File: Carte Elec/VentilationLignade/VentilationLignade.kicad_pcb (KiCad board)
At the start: 2 copper layers, 28 parts, among them P1 RelaisBoard1, P10 SDCard, P11 Codeur Rotatif, P12 Teensy dessous, P13 EndStops1, P14 Teensy_Haut, P15 EndStops2, P16 Teensy_cote, P17 Retour 12V, P18 Masse_12V, P19 12V1, P2 Temp_Ext, P20 12V2, P21 12V_1et2, P22 Teensy_Bas, P3 RelaisBoard2, P4 Temp_Int, P5 RelaisBoard3, P6 Temp_Chem, P7 RelaisBoard4, P8 RelaisBoard5, P9 TFT, SW1 Reset_Push, SW2 BackLight_On/ff

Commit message: Dessin de carte. Changement des pins pour avoir un truc cohérent au niveau de la carte.
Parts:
- C1, C2, C3: moved to B.Cu
- moved P12 216.8 mm to (0.00, 0.00)
- moved P18 114.1 mm to (262.9, 200.7)
- moved P19 102.6 mm to (269.2, 157.5), turned to 90 degrees
- moved P20 101.3 mm to (269.2, 149.9), turned to 90 degrees
- moved P21 97.1 mm to (241.3, 200.7), turned to 180 degrees
- moved P17 88.0 mm to (256.5, 143.5)
- moved P15 81.6 mm to (250.2, 143.5)
- moved P13 75.3 mm to (243.8, 143.5)
- moved P8 73.3 mm to (203.2, 200.7), turned to 180 degrees
- moved SW2 70.4 mm to (231.1, 168.9), turned to 90 degrees
- moved P7 68.3 mm to (190.5, 200.7), turned to 180 degrees
- moved P1 66.8 mm to (152.4, 200.7), turned to 180 degrees
- moved P5 65.4 mm to (177.8, 200.7), turned to 180 degrees
- moved P3 64.9 mm to (165.1, 200.7), turned to 180 degrees
- moved R1 60.2 mm to (222.2, 163.8), turned to 270 degrees
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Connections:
- P12 pad 1: 12V2_ON -> SELECT_12V
- P12 pad 10: ENCODEUR_B -> (no net)
- P12 pad 2: SELECT_12V -> (no net)
- P12 pad 3: 12V1_ON -> ENCODEUR_SW
- P12 pad 4: 12V_CHECK -> ENCODEUR_A
- P12 pad 5: SELECT_VMC -> ENCODEUR_B
- P12 pad 6: ENCODEUR_SW -> (no net)
- P12 pad 7: VENT_CAVE -> (no net)
- P12 pad 8: ENCODEUR_A -> (no net)
- P12 pad 9: VENT_CHEMINEE -> (no net)
- P14 pad 1: (no net) -> 12V_CHECK
- P22 pad 10: (no net) -> 12V2_ON
- P22 pad 2: (no net) -> BYPASS_1_F
- P22 pad 3: (no net) -> BYPASS_1_O
- P22 pad 4: (no net) -> BYPASS_2_F
- P22 pad 5: BYPASS_1_F -> BYPASS_2_O
- P22 pad 6: BYPASS_1_O -> VENT_CAVE
- P22 pad 7: BYPASS_2_F -> VENT_CHEMINEE
- P22 pad 8: BYPASS_2_O -> 12V1_ON
- P22 pad 9: (no net) -> SELECT_VMC
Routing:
- net GND: track 0.00 -> 230.6 mm, vias 0 -> 1
- net +5V: track 0.00 -> 165.6 mm
- net +3.3V: track 0.00 -> 129.4 mm
- net SPI_MISO: track 0.00 -> 116.7 mm
- net SPI_SCK: track 0.00 -> 83.7 mm
- net GNDPWR: track 0.00 -> 79.3 mm
- net 12V2: track 0.00 -> 69.4 mm
- net 12V1: track 0.00 -> 60.4 mm
- net TFT_DC: track 0.00 -> 47.4 mm
- net SPI_MOSI: track 0.00 -> 43.0 mm
- net TFT_CS: track 0.00 -> 36.2 mm
- net TEXT_CS: track 0.00 -> 30.4 mm
- net SELECT_VMC: track 0.00 -> 30.1 mm
- net BYPASS_1_O: track 0.00 -> 30.1 mm
- net BYPASS_1_F: track 0.00 -> 30.1 mm
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- added copper zone on F.Cu, net GND
- added copper zone on F.Cu, net GNDPWR
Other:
- net class 12V added: clearance 0.3, trace_width 1, via_dia 0.889, via_drill 0.635

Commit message: Ajout d'un RS232 MAX au cas ou.
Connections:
- P12 pad 2: (no net) -> ENCODEUR_SW
- P12 pad 3: ENCODEUR_SW -> (no net)
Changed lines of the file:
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@@
     (links 76)
     (no_connects 11)
-    (area 0 0 0 0)
+    (area -10.650501 -4.8085 271.830001 204.520001)
     (thickness 1.6)
     (drawings 4)
@@
     (pad 2 thru_hole circle (at -5.08 3.81) (size 1.397 1.397) (drill 0.8128)
       (layers *.Cu *.Mask Dessus.SilkS)
+      (net 14 ENCODEUR_SW)
     )
     (pad 3 thru_hole circle (at -2.54 3.81) (size 1.397 1.397) (drill 0.8128)
       (layers *.Cu *.Mask Dessus.SilkS)
-      (net 14 ENCODEUR_SW)
     )
     (pad 4 thru_hole circle (at 0 3.81) (size 1.397 1.397) (drill 0.8128)
@@
   (segment (start 157.48 203.2) (end 166.37 203.2) (width 0.254) (layer Dessus.Cu) (net 19))
   (segment (start 156.21 201.93) (end 157.48 203.2) (width 0.254) (layer Dessus.Cu) (net 19))
-  (segment (start 266.7 200.66) (end 268.605 198.755) (width 1) (layer Dessus.Cu) (net 20) (status 400000))
+  (segment (start 266.7 200.66) (end 268.605 198.755) (width 1) (layer Dessus.Cu) (net 20))
   (segment (start 271.145 161.29) (end 271.145 154.305) (width 1) (layer Dessus.Cu) (net 20))
   (segment (start 268.605 163.83) (end 271.145 161.29) (width 1) (layer Dessus.Cu) (net 20))
   (segment (start 268.605 198.755) (end 268.605 163.83) (width 1) (layer Dessus.Cu) (net 20))
-  (segment (start 264.16 200.66) (end 266.7 200.66) (width 1) (layer Dessus.Cu) (net 20) (status C00000))
-  (segment (start 261.62 200.66) (end 264.16 200.66) (width 1) (layer Dessus.Cu) (net 20) (status C00000))
-  (segment (start 259.08 200.66) (end 261.62 200.66) (width 1) (layer Dessus.Cu) (net 20) (status C00000))
+  (segment (start 264.16 200.66) (end 266.7 200.66) (width 1) (layer Dessus.Cu) (net 20))
+  (segment (start 261.62 200.66) (end 264.16 200.66) (width 1) (layer Dessus.Cu) (net 20))
+  (segment (start 259.08 200.66) (end 261.62 200.66) (width 1) (layer Dessus.Cu) (net 20))
   (segment (start 269.24 148.59) (end 270.51 148.59) (width 1) (layer Dessus.Cu) (net 20))
   (segment (start 270.51 148.59) (end 271.145 149.225) (width 1) (layer Dessus.Cu) (net 20))

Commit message: Reprise de la carte => Dimensions réduites 50x100mm
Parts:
- added C4: C, C2, F.Cu at (195.6, 248.9)
- added C5: C, C2, F.Cu at (227.1, 251.0)
- added C7: C, C2, F.Cu at (213.6, 264.2)
- added C8: C, C2, F.Cu at (221.0, 264.2)
- added P23: Serial, SIL-4, F.Cu at (223.5, 254.0)
- added P24: Temp_PuitC, SIL-5, F.Cu at (198.1, 219.7)
- added R2: R, R4, F.Cu at (232.7, 253.5)
- added R3: R, R4, F.Cu at (229.9, 253.5)
- added U1: MAX232, SO16W, F.Cu at (216.4, 256.5)
- C1, C2, C3: moved to F.Cu
- P12: value Teensy dessous -> Teensy Bottom; footprint DIP-14__300 -> SIL-10
- moved P12 316.0 mm to (188.0, 254.0)
- moved P20 81.1 mm to (243.2, 226.7)
- moved P19 79.9 mm to (243.2, 233.0)
- moved P13 78.1 mm to (226.7, 219.7)
- moved P15 78.1 mm to (233.0, 219.7)
- moved P17 78.1 mm to (239.4, 219.7)
- moved P10 77.7 mm to (195.6, 233.7)
- moved P2 76.9 mm to (184.2, 219.7)
- moved P4 76.9 mm to (170.2, 219.7)
- moved P6 76.9 mm to (156.2, 219.7)
- moved P9 76.2 mm to (203.2, 238.8)
- moved SW2 74.5 mm to (213.4, 241.3)
- moved C1 74.4 mm to (208.0, 258.3), turned to 0 degrees
- moved R1 73.7 mm to (208.3, 236.2)
- moved C2 70.7 mm to (208.0, 255.5), turned to 0 degrees
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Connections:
- P12 pad 2: ENCODEUR_SW -> ENCODEUR_A
- P12 pad 3: (no net) -> ENCODEUR_B
- P12 pad 4: ENCODEUR_A -> ENCODEUR_SW
- P12 pad 5: ENCODEUR_B -> RX
- P12 pad 6: (no net) -> TX
- P14 pad 7: (no net) -> TPUIT_CS
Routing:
- net ENDSTOP_2_2: track 0.00 -> 68.2 mm
- net ENDSTOP_2_1: track 0.00 -> 68.0 mm
- net 12V_CHECK: track 0.00 -> 66.8 mm
- net ENDSTOP_1_1: track 0.00 -> 66.3 mm
- net ENDSTOP_1_2: track 0.00 -> 66.2 mm
- net GND: track 230.6 -> 279.9 mm, vias 1 -> 0
- net 12V2_ON: track 0.00 -> 43.9 mm
- net TPUIT_CS: track 0.00 -> 42.7 mm
- net RX: track 0.00 -> 34.0 mm, vias 0 -> 1
- net TX: track 0.00 -> 33.0 mm, vias 0 -> 1
- net ENCODEUR_A: track 4.48 -> 35.5 mm
- net SELECT_12V: track 0.00 -> 30.8 mm
- net ENCODEUR_B: track 3.96 -> 31.2 mm
- net N-0000023: track 0.00 -> 25.5 mm
- net ENCODEUR_SW: track 3.43 -> 28.4 mm
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- added copper zone on B.Cu, net +3.3V
- added copper zone on B.Cu, net +5V
- removed copper zone on F.Cu, net GNDPWR
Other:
- net class 12V: clearance 0.3 -> 0.5; via_dia 0.889 -> 1.2
- net class Default: clearance 0.254 -> 0.35; trace_width 0.254 -> 0.35; via_dia 0.889 -> 1.2; via_drill 0.635 -> 0.8
- rule trace_clearance: 0.254 -> 0.35

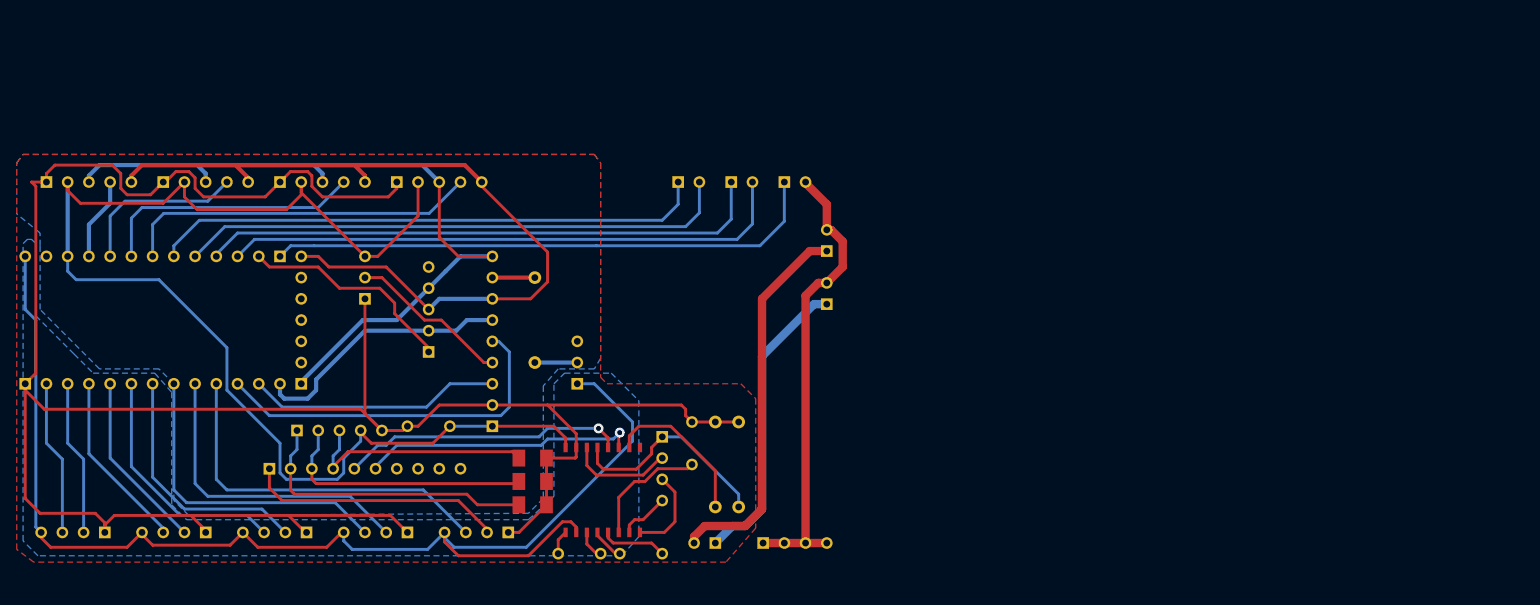
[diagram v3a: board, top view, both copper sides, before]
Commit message: Reprise de carte  : Suppression MAX232, pour avoir la place de mettre les MOC207
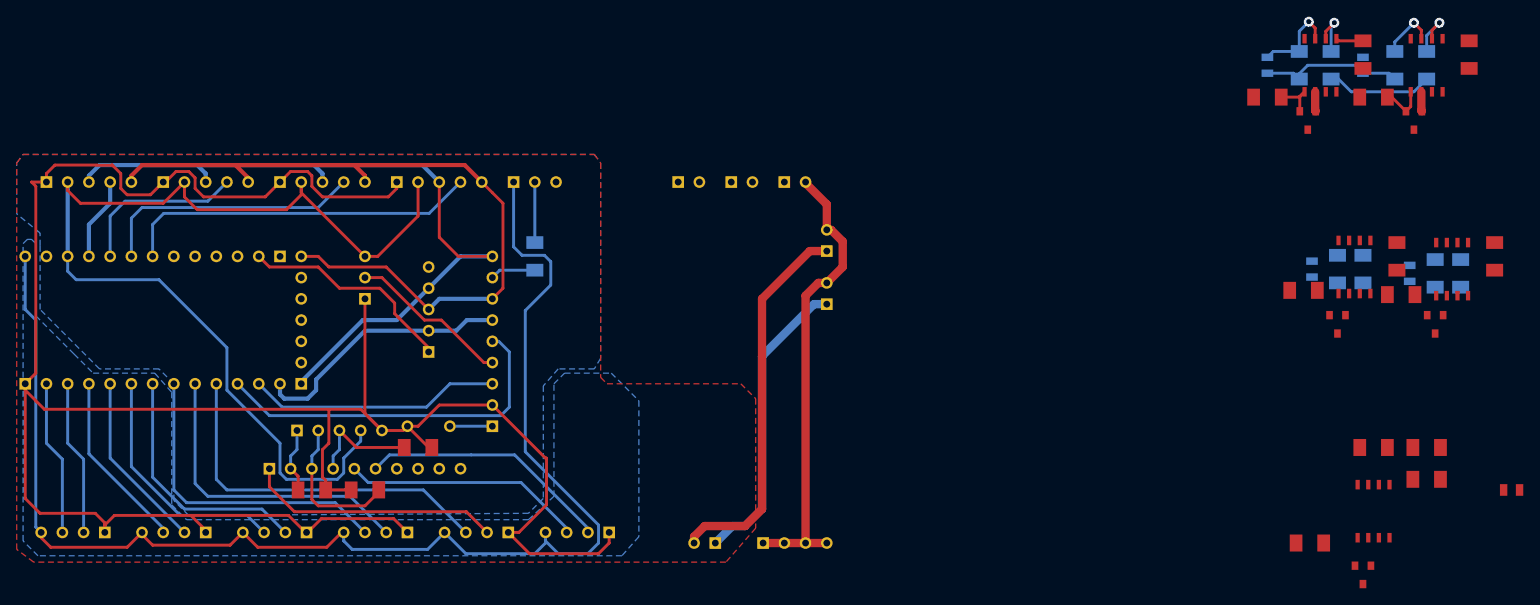
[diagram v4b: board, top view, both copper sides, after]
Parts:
- removed C5, C7, C8: C, C2
- removed R2, R3: R, R4
- removed U1: MAX232, SO16W
- added C10: C, SM0805, B.Cu at (312.9, 230.6)
- added C11: C, SM0805, F.Cu at (325.1, 256.5)
- added C12: C, SM0805, B.Cu at (295.9, 205.7)
- added C13: C, SM0805, B.Cu at (307.3, 205.7)
- added C9: C, SM0805, B.Cu at (301.2, 230.1)
- added D1: DIODE, SOT23, F.Cu at (304.3, 236.7)
- added D2: DIODE, SOT23, F.Cu at (316.0, 236.7)
- added D3: DIODE, SOT23, F.Cu at (307.3, 266.7)
- added D4: DIODE, SOT23, F.Cu at (300.7, 212.3)
- added D5: DIODE, SOT23, F.Cu at (313.4, 212.3)
- added R10: R, SM1206, B.Cu at (316.0, 230.6)
- added R11: R, SM1206, F.Cu at (315.0, 251.5)
- added R12: R, SM1206, B.Cu at (299.7, 205.7)
- added R13: R, SM1206, B.Cu at (311.1, 205.7)
- added R14: R, SM1206, B.Cu at (307.3, 230.1)
- added R15: R, SM1206, B.Cu at (319.0, 230.6)
- added R16: R, SM1206, F.Cu at (308.6, 251.5)
- added R17: R, SM1206, B.Cu at (303.5, 205.7)
- added R18: R, SM1206, B.Cu at (315.0, 205.7)
- added R19: R, SM1206, F.Cu at (311.4, 228.6)
- added R20: R, SM1206, F.Cu at (323.1, 228.6)
- added R21: R, SM1206, F.Cu at (315.0, 255.3)
- added R22: R, SM1206, F.Cu at (307.3, 204.5)
- added R23: R, SM1206, F.Cu at (320.0, 204.5)
- added R4: R, SM1206, F.Cu at (300.2, 232.7)
- added R5: R, SM1206, F.Cu at (311.9, 233.2)
- added R6: R, SM1206, F.Cu at (301.0, 262.9)
- added R7: R, SM1206, F.Cu at (295.9, 209.6)
- added R8: R, SM1206, F.Cu at (308.6, 209.6)
- added R9: R, SM1206, B.Cu at (304.3, 230.1)
- added U2: OPTO-TRANSISTOR, SO8N, F.Cu at (306.3, 229.9)
- added U3: OPTO-TRANSISTOR, SO8N, F.Cu at (318.0, 230.1)
- added U4: OPTO-TRANSISTOR, SO8N, F.Cu at (308.6, 259.1)
- added U5: OPTO-TRANSISTOR, SO8N, F.Cu at (302.3, 205.7)
- added U6: OPTO-TRANSISTOR, SO8N, F.Cu at (315.0, 205.7)
- R1: footprint R4 -> SM1206; moved to B.Cu
- moved C1 26.5 mm to (181.6, 256.5)
- moved SW2 22.2 mm to (208.3, 219.7), turned to 0 degrees
- moved C2 20.1 mm to (188.0, 256.5), turned to 180 degrees
- moved C3 13.8 mm to (194.3, 251.5)
- moved P23 12.7 mm to (213.4, 261.6), turned to 180 degrees
- moved R1 7.62 mm to (208.3, 228.6), turned to 90 degrees
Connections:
- P13 pad 1: ENDSTOP_1_1 -> /Optocouplers/END_1_1
- P13 pad 2: ENDSTOP_1_2 -> /Optocouplers/END_1_2
- P15 pad 1: ENDSTOP_2_1 -> /Optocouplers/END_2_1
- P15 pad 2: ENDSTOP_2_2 -> /Optocouplers/END_2_2
- P17 pad 1: 12V_CHECK -> /Optocouplers/12V_IN
- P23 pad 1: N-0000023 -> GND
- P23 pad 2: N-0000031 -> TX
- P23 pad 3: N-0000022 -> RX
- P23 pad 4: N-0000030 -> +5V
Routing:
- net ENDSTOP_2_1: track 68.0 -> 0.00 mm
- net ENDSTOP_1_1: track 66.3 -> 0.00 mm
- net ENDSTOP_1_2: track 66.2 -> 0.00 mm
- net ENDSTOP_2_2: track 68.2 -> 5.91 mm, vias 0 -> 1
- net 12V_CHECK: track 66.8 -> 6.33 mm, vias 0 -> 1
- net ENCODEUR_A: track 35.5 -> 7.80 mm
- net N-0000023: track 25.5 -> 0.00 mm
- net N-0000038: track 18.7 -> 0.00 mm
- net +5V: track 148.9 -> 164.0 mm
- net ENCODEUR_SW: track 28.4 -> 13.5 mm
- net GND: track 279.9 -> 294.7 mm
- net N-0000036: track 14.6 -> 0.00 mm
- net ENCODEUR_B: track 31.2 -> 17.8 mm
- net N-0000031: track 12.5 -> 0.00 mm
- net N-0000057: track 0.00 -> 10.5 mm, vias 0 -> 1
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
